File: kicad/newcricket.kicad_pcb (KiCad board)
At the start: 2 copper layers, 32.5 x 49 mm, 25 parts, among them IC1 ATTINY85-P, Q1 Q_NPN_BCE, SW1 SW_PUSH, SW2 SW_PUSH, SW3 SWITCH_INV, U1 LM335

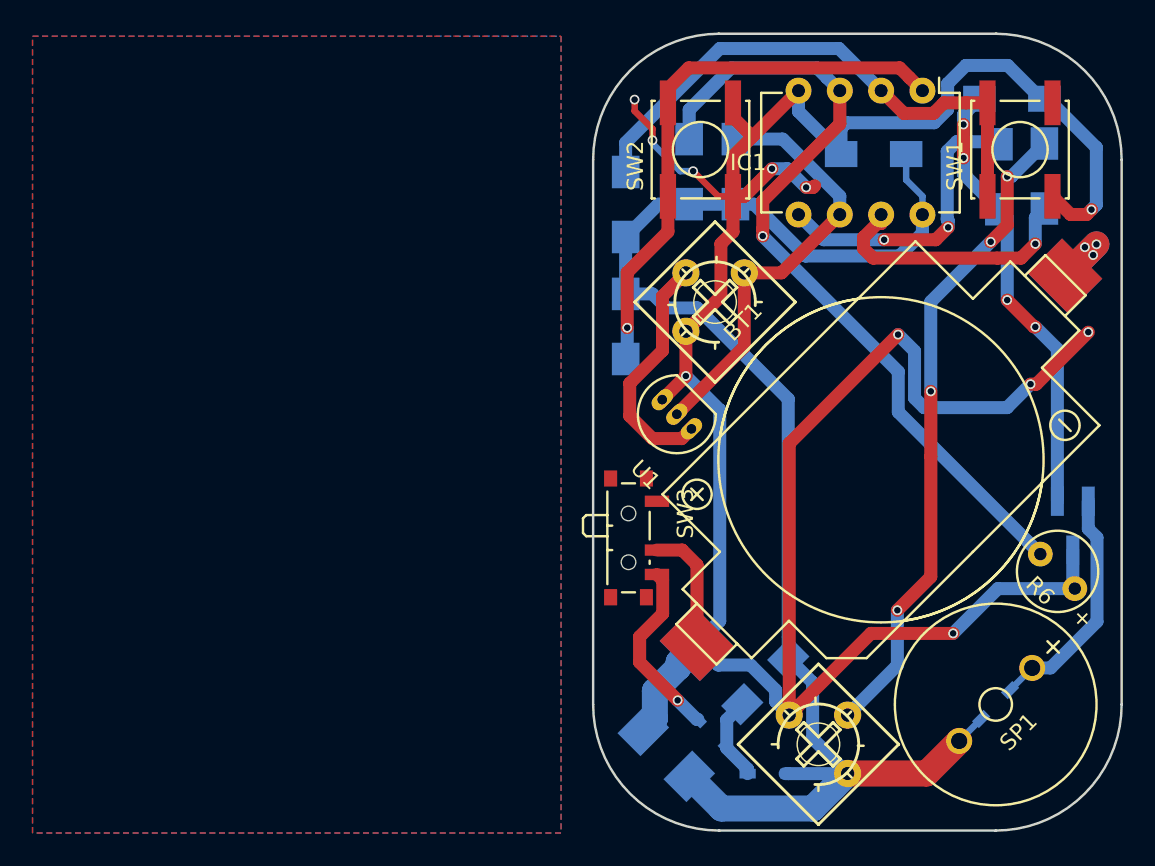
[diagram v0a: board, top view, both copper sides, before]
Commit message: Rearranged traces on upper half of board. Also moved around silkscreen labels.
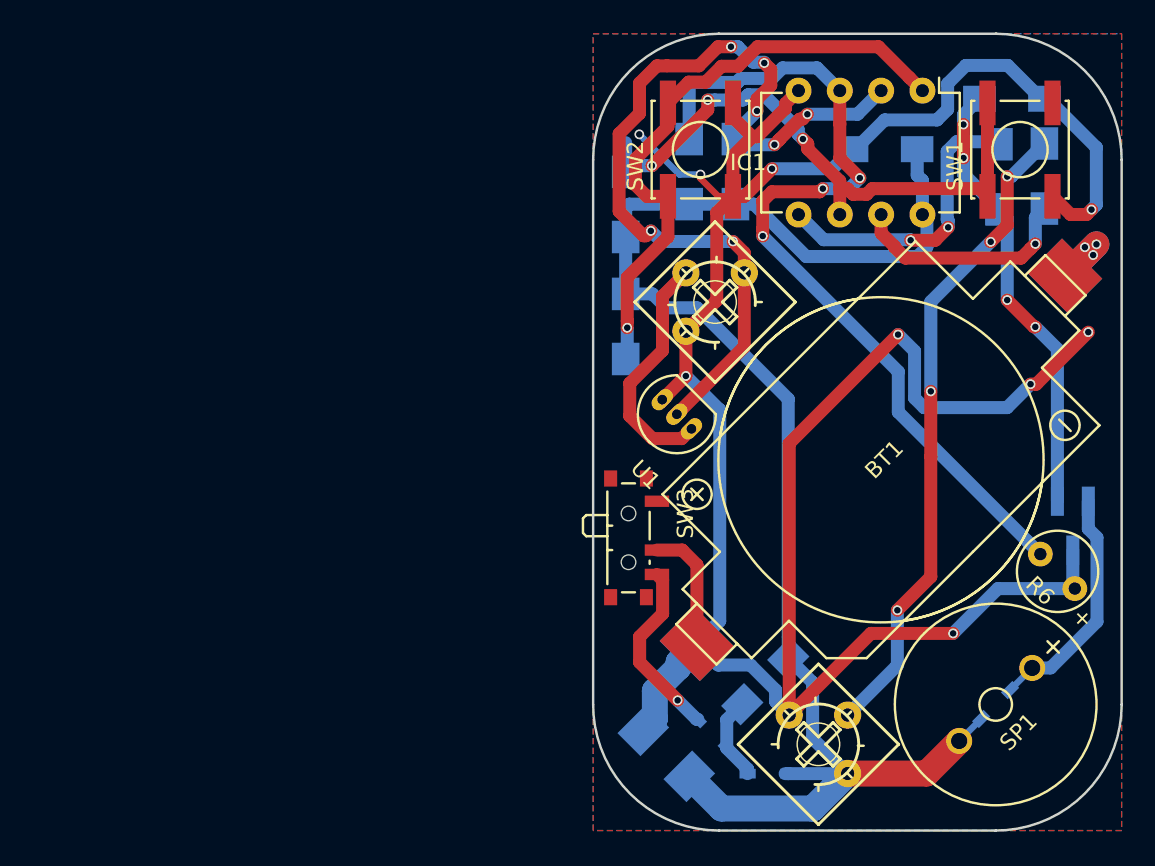
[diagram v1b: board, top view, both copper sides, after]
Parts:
- moved C3 0.74 mm to (92.1, 71.6)
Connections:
- R2 pad 2: Net-(IC1-Pad2) -> Net-(IC1-Pad6)
- R4 pad 2: Net-(IC1-Pad6) -> Net-(IC1-Pad2)
- RV2 pad 3: Net-(IC1-Pad6) -> Net-(IC1-Pad2)
- SW1 pad 1: Net-(IC1-Pad2) -> Net-(IC1-Pad6)
- U1 pad 2: Net-(IC1-Pad6) -> Net-(IC1-Pad2)
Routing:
- net Net-(IC1-Pad2): track 34.1 -> 54.3 mm, vias 0 -> 7
- net Net-(IC1-Pad6): track 26.8 -> 37.2 mm, vias 0 -> 3
- net GND: track 174.5 -> 168.7 mm, vias 11 -> 9
- net Net-(IC1-Pad3): track 50.2 -> 55.4 mm, vias 2 -> 4
- net Net-(IC1-Pad1): track 36.4 -> 39.4 mm
- net Net-(IC1-Pad7): track 16.2 -> 14.0 mm
- net VCC: track 91.9 -> 93.9 mm
